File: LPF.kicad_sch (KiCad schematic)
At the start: 41 parts

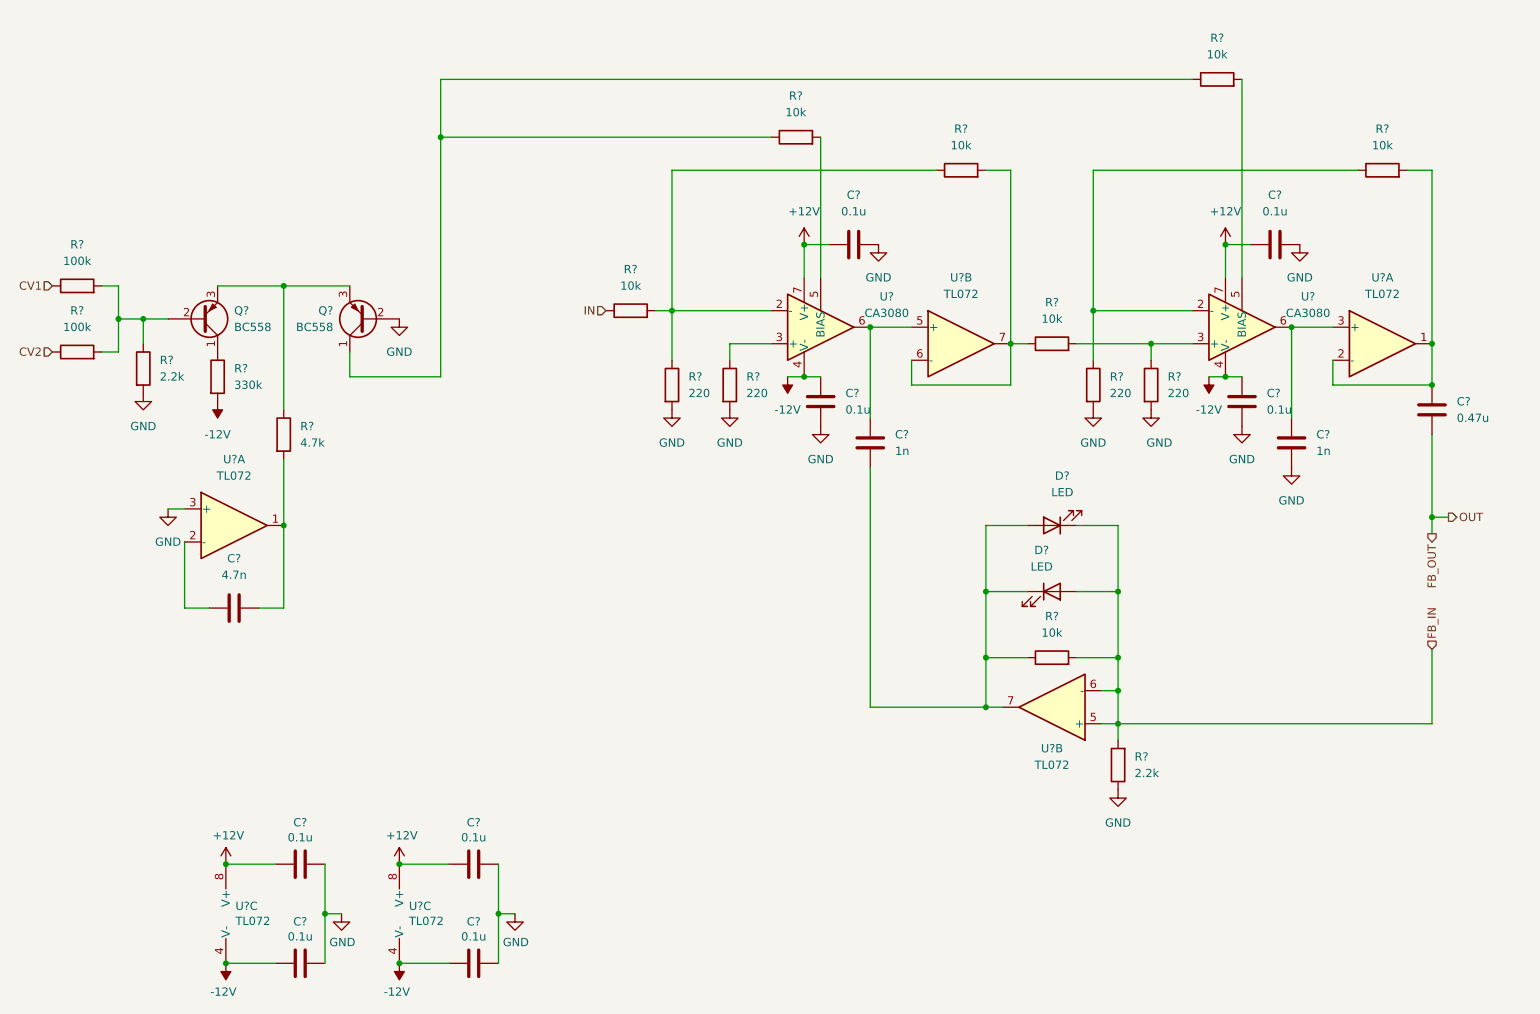
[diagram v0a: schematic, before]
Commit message: Finish schematic
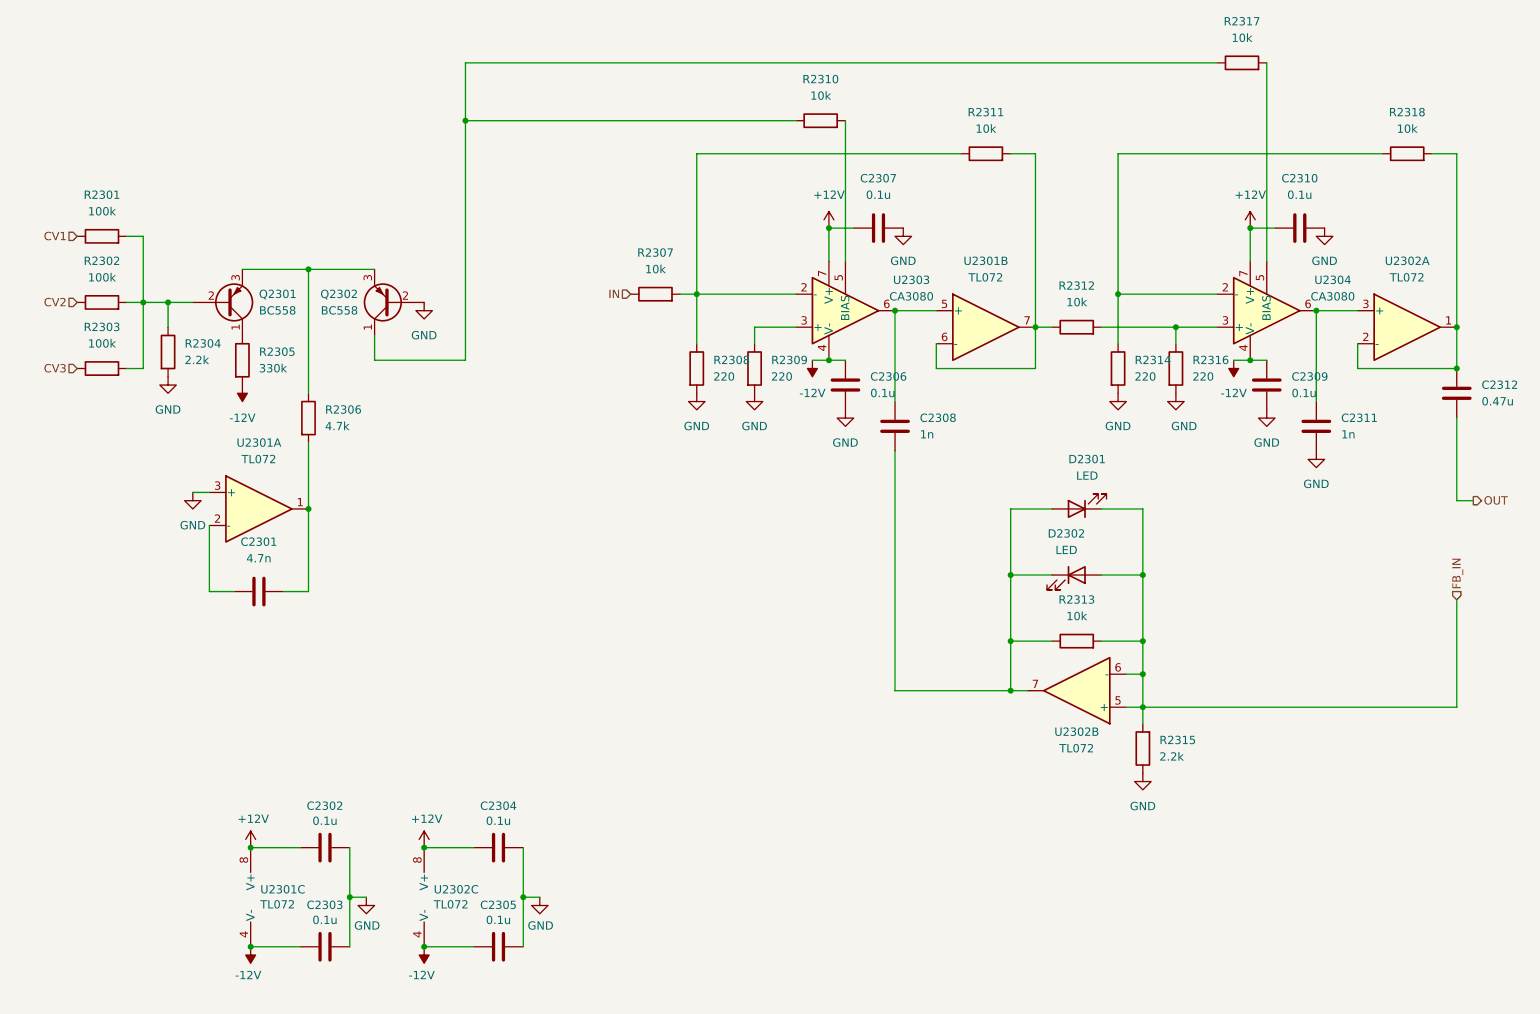
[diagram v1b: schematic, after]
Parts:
- removed C? (x2): 1n, symbol Device:C
- removed C? (x4): 0.1u, symbol Device:C
- removed C? (x4): 0.1u, Capacitor_THT:C_Disc_D5.0mm_W2.5mm_P5.00mm, symbol Device:C
- removed C?: 4.7n, symbol Device:C
- removed C?: 0.47u, symbol Device:C
- removed D? (x2): LED, symbol Device:LED
- removed Q? (x2): BC558, Package_TO_SOT_THT:TO-92_Inline, symbol Transistor_BJT:BC558
- removed R? (x2): 100k, symbol Device:R
- removed R? (x2): 2.2k, symbol Device:R
- removed R? (x4): 220, symbol Device:R
- removed R? (x7): 10k, symbol Device:R
- removed R?: 4.7k, symbol Device:R
- removed R?: 330k, symbol Device:R
- removed U? (x4): TL072, symbol Amplifier_Operational:TL072
- removed U? (x2): CA3080, symbol Amplifier_Operational:CA3080
- removed U? (x2): TL072, Package_DIP:DIP-8_W7.62mm_Socket, symbol Amplifier_Operational:TL072
- added C2301: 4.7n, Capacitor_THT:C_Disc_D5.0mm_W2.5mm_P5.00mm, symbol Device:C
- added C2302, C2303, C2304, C2305, C2306, C2307, C2309, C2310: 0.1u, Capacitor_THT:C_Disc_D5.0mm_W2.5mm_P5.00mm, symbol Device:C
- added C2308, C2311: 1n, Capacitor_THT:C_Disc_D5.0mm_W2.5mm_P5.00mm, symbol Device:C
- added C2312: 0.47u, Capacitor_THT:C_Disc_D5.0mm_W2.5mm_P5.00mm, symbol Device:C
- added D2301, D2302: LED, LED_THT:LED_D5.0mm, symbol Device:LED
- added Q2301, Q2302: BC558, Package_TO_SOT_THT:TO-92_HandSolder, symbol Transistor_BJT:BC558
- added R2301, R2302, R2303: 100k, Resistor_THT:R_Axial_DIN0207_L6.3mm_D2.5mm_P7.62mm_Horizontal, symbol Device:R
- added R2304, R2315: 2.2k, Resistor_THT:R_Axial_DIN0207_L6.3mm_D2.5mm_P7.62mm_Horizontal, symbol Device:R
- added R2305: 330k, Resistor_THT:R_Axial_DIN0207_L6.3mm_D2.5mm_P7.62mm_Horizontal, symbol Device:R
- added R2306: 4.7k, Resistor_THT:R_Axial_DIN0207_L6.3mm_D2.5mm_P7.62mm_Horizontal, symbol Device:R
- added R2307, R2310, R2311, R2312, R2313, R2317, R2318: 10k, Resistor_THT:R_Axial_DIN0207_L6.3mm_D2.5mm_P7.62mm_Horizontal, symbol Device:R
- added R2308, R2309, R2314, R2316: 220, Resistor_THT:R_Axial_DIN0207_L6.3mm_D2.5mm_P7.62mm_Horizontal, symbol Device:R
- added U2301, U2302: TL072, Package_DIP:DIP-8_W7.62mm_Socket, symbol Amplifier_Operational:TL072
- added U2303, U2304: CA3080, Package_DIP:DIP-8_W7.62mm_Socket, symbol Amplifier_Operational:CA3080
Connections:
- net +12V: now also C2302.1, C2304.1, C2307.2, C2310.2, U2301.8 (V+), U2302.8 (V+), U2303.7 (V+), U2304.7 (V+)
- net -12V: now also C2303.1, C2305.1, C2306.2, C2309.2, R2305.2, U2301.4 (V-), U2302.4 (V-), U2303.4 (V-), U2304.4 (V-)
- net CV1: now also R2301.1
- net CV2: now also R2302.1
- net FB_IN: now also D2301.1 (K), D2302.2 (A), R2313.2, R2315.2, U2302.5 (+), U2302.6 (-)
- net GND: now also C2302.2, C2303.2, C2304.2, C2305.2, C2306.1, C2307.1, C2309.1, C2310.1, C2311.2, Q2302.2 (B), R2304.2, R2308.2, R2309.2, R2314.2, R2315.1, R2316.2, U2301.3 (+)
- net IN: now also R2307.1
- new net: C2308.2, D2301.2 (A), D2302.1 (K), R2313.1, U2302.7
- new net: C2308.1, U2301.5 (+), U2303.6
- new net: R2311.2, R2312.1, U2301.6 (-), U2301.7
- new net: R2309.1, U2303.3 (+)
- new net: Q2301.1 (C), R2305.1
- new net: R2312.2, R2316.1, U2304.3 (+)
- new net: Q2302.1 (C), R2310.1, R2317.1
- new net: Q2301.3 (E), Q2302.3 (E), R2306.1
- new net: R2307.2, R2308.1, R2311.1, U2303.2 (-)
- new net: Q2301.2 (B), R2301.2, R2302.2, R2303.2, R2304.1
- new net: C2311.1, U2302.3 (+), U2304.6
- new net: C2312.1, R2318.2, U2302.1, U2302.2 (-)
- new net: R2317.2, U2304.5 (BIAS)
- new net: R2314.1, R2318.1, U2304.2 (-)
- new net: C2301.1, U2301.2 (-)
- new net: C2301.2, R2306.2, U2301.1
- new net: R2310.2, U2303.5 (BIAS)
- new net CV3: R2303.1
- new net OUT: C2312.2

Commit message: Finish PCB
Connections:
- net FB_IN: no longer D2301.1 (K), D2302.2 (A), R2313.2, R2315.2, U2302.6 (-)
- net at Q2301.1 (C), R2305.1: now also C2301.1, U2301.2 (-)
- new net: D2301.1 (K), D2302.2 (A), R2313.2, R2315.2, U2302.6 (-)
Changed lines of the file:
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@@
   (junction (at 57.15 69.85) (diameter 0) (color 0 0 0 0)
   )
+  (junction (at 68.58 74.93) (diameter 0) (color 0 0 0 0)
+  )
   (junction (at 207.01 127) (diameter 0) (color 0 0 0 0)
   )
@@
   (junction (at 186.69 129.54) (diameter 0) (color 0 0 0 0)
   )
+  (junction (at 63.5 114.3) (diameter 0) (color 0 0 0 0)
+  )
   (junction (at 186.69 121.92) (diameter 0) (color 0 0 0 0)
   )
   (junction (at 96.52 168.91) (diameter 0) (color 0 0 0 0)
   )
-  (junction (at 207.01 132.08) (diameter 0) (color 0 0 0 0)
-  )
   (junction (at 111.76 161.29) (diameter 0) (color 0 0 0 0)
   )
+  (wire (pts (xy 63.5 74.93) (xy 68.58 74.93))
+    (stroke (width 0) (type default) (color 0 0 0 0))
+  )
   (wire (pts (xy 212.09 76.2) (xy 212.09 73.66))
     (stroke (width 0) (type default) (color 0 0 0 0))
@@
     (stroke (width 0) (type default) (color 0 0 0 0))
   )
+  (wire (pts (xy 63.5 92.71) (xy 63.5 74.93))
+    (stroke (width 0) (type default) (color 0 0 0 0))
+  )
   (wire (pts (xy 220.98 78.74) (xy 223.52 78.74))
     (stroke (width 0) (type default) (color 0 0 0 0))
   )
-  (wire (pts (xy 207.01 132.08) (xy 207.01 134.62))
-    (stroke (width 0) (type default) (color 0 0 0 0))
-  )
   (wire (pts (xy 147.32 73.66) (xy 153.67 73.66))
     (stroke (width 0) (type default) (color 0 0 0 0))
@@
     (stroke (width 0) (type default) (color 0 0 0 0))
   )
+  (wire (pts (xy 55.88 92.71) (xy 63.5 92.71))
+    (stroke (width 0) (type default) (color 0 0 0 0))
+  )
   (wire (pts (xy 102.87 41.91) (xy 153.67 41.91))
     (stroke (width 0) (type default) (color 0 0 0 0))
@@
     (stroke (width 0) (type default) (color 0 0 0 0))
   )
+  (wire (pts (xy 63.5 114.3) (xy 55.88 114.3))
+    (stroke (width 0) (type default) (color 0 0 0 0))
+  )
   (wire (pts (xy 190.5 80.01) (xy 190.5 73.66))
     (stroke (width 0) (type default) (color 0 0 0 0))
@@
     (stroke (width 0) (type default) (color 0 0 0 0))
   )
-  (wire (pts (xy 207.01 127) (xy 207.01 132.08))
-    (stroke (width 0) (type default) (color 0 0 0 0))
-  )
   (wire (pts (xy 255.27 115.57) (xy 255.27 132.08))
     (stroke (width 0) (type default) (color 0 0 0 0))
@@
     (stroke (width 0) (type default) (color 0 0 0 0))
   )
-  (wire (pts (xy 207.01 132.08) (xy 204.47 132.08))
+  (wire (pts (xy 204.47 132.08) (xy 255.27 132.08))
     (stroke (width 0) (type default) (color 0 0 0 0))
   )
@@
     (stroke (width 0) (type default) (color 0 0 0 0))
   )
+  (wire (pts (xy 207.01 127) (xy 207.01 134.62))
+    (stroke (width 0) (type default) (color 0 0 0 0))
+  )
   (wire (pts (xy 207.01 101.6) (xy 207.01 111.76))
     (stroke (width 0) (type default) (color 0 0 0 0))
@@
     (stroke (width 0) (type default) (color 0 0 0 0))
   )
-  (wire (pts (xy 255.27 132.08) (xy 207.01 132.08))
-    (stroke (width 0) (type default) (color 0 0 0 0))
-  )
+  (wire (pts (xy 55.88 114.3) (xy 55.88 92.71))
+    (stroke (width 0) (type default) (color 0 0 0 0))
+  )
